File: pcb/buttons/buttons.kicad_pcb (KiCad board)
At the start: 2 copper layers, 24 parts, among them SW1 SW_Push, SW2 SW_Push, SW3 SW_Push, SW4 SW_Push, SW5 SW_Push, SW6 SW_Push, SW7 SW_Push, SW8 SW_Push

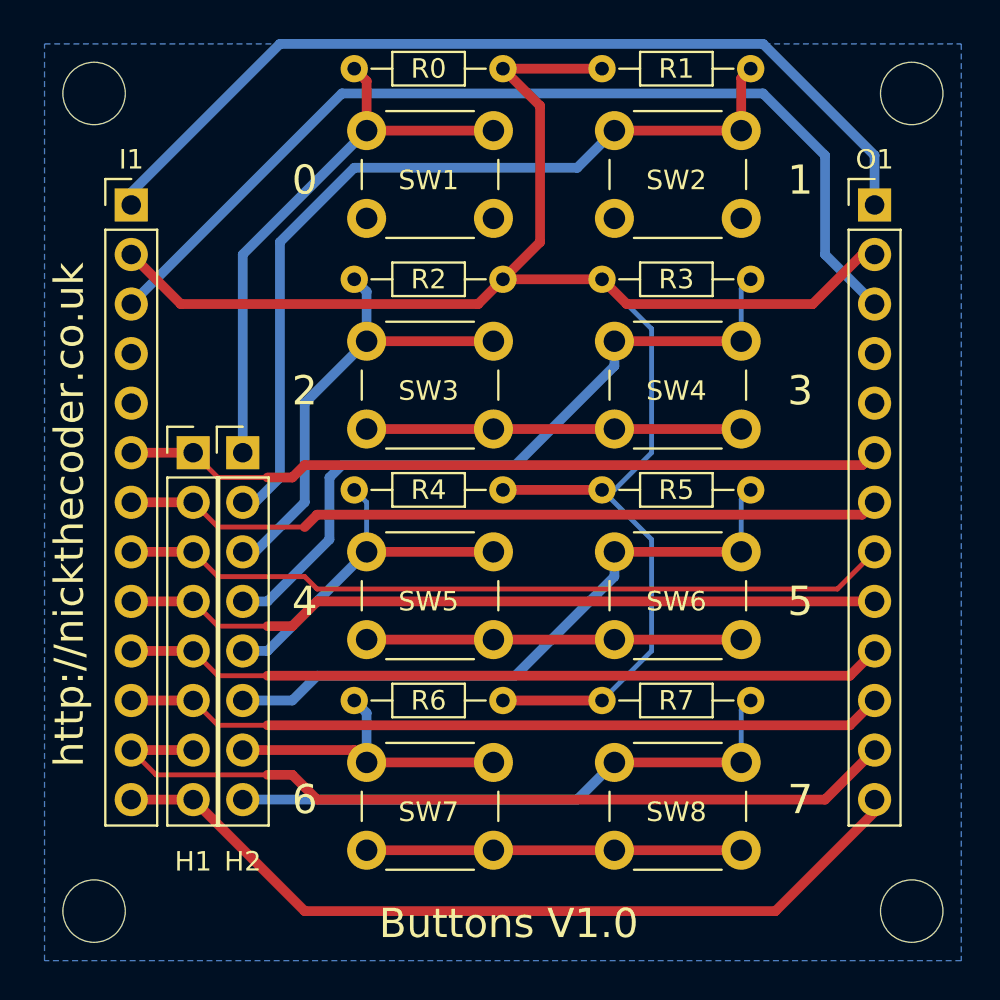
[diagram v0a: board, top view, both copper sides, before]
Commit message: Tidied up old thinner tracks.
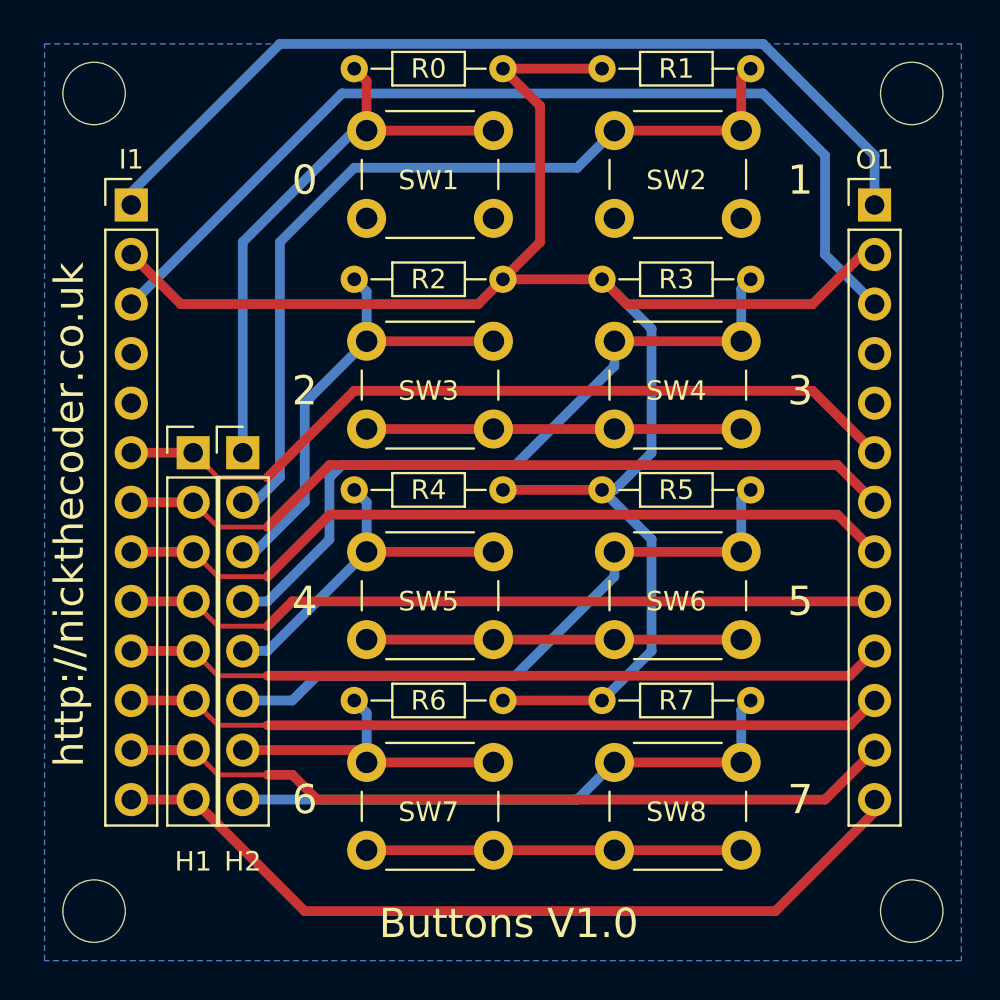
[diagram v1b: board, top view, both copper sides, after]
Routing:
- net /VIN: track 93.6 -> 47.4 mm
- net /VCC: track 135.5 -> 98.1 mm
- net /3V3: track 84.8 -> 50.0 mm
- net /L3: track 69.5 -> 39.2 mm
- net /L4: track 69.0 -> 39.2 mm
- net /L5: track 69.0 -> 39.2 mm
- net /L6: track 72.5 -> 43.3 mm
- net /L0: track 69.5 -> 41.8 mm
- net /L1: track 68.0 -> 40.7 mm
- net Net-(H2-Pad3): track 37.8 -> 24.6 mm
- net Net-(H2-Pad1): track 39.0 -> 30.3 mm
- net /L7: track 75.2 -> 68.0 mm
- net Net-(H2-Pad5): track 25.6 -> 18.4 mm
- net /L2: track 39.7 -> 40.7 mm
- net Net-(H2-Pad7): track 19.2 -> 18.3 mm
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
